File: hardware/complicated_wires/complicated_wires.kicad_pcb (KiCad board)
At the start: 2 copper layers, 80 x 80 mm, 37 parts, among them J1 JST_XH_4P, U1 Pico2

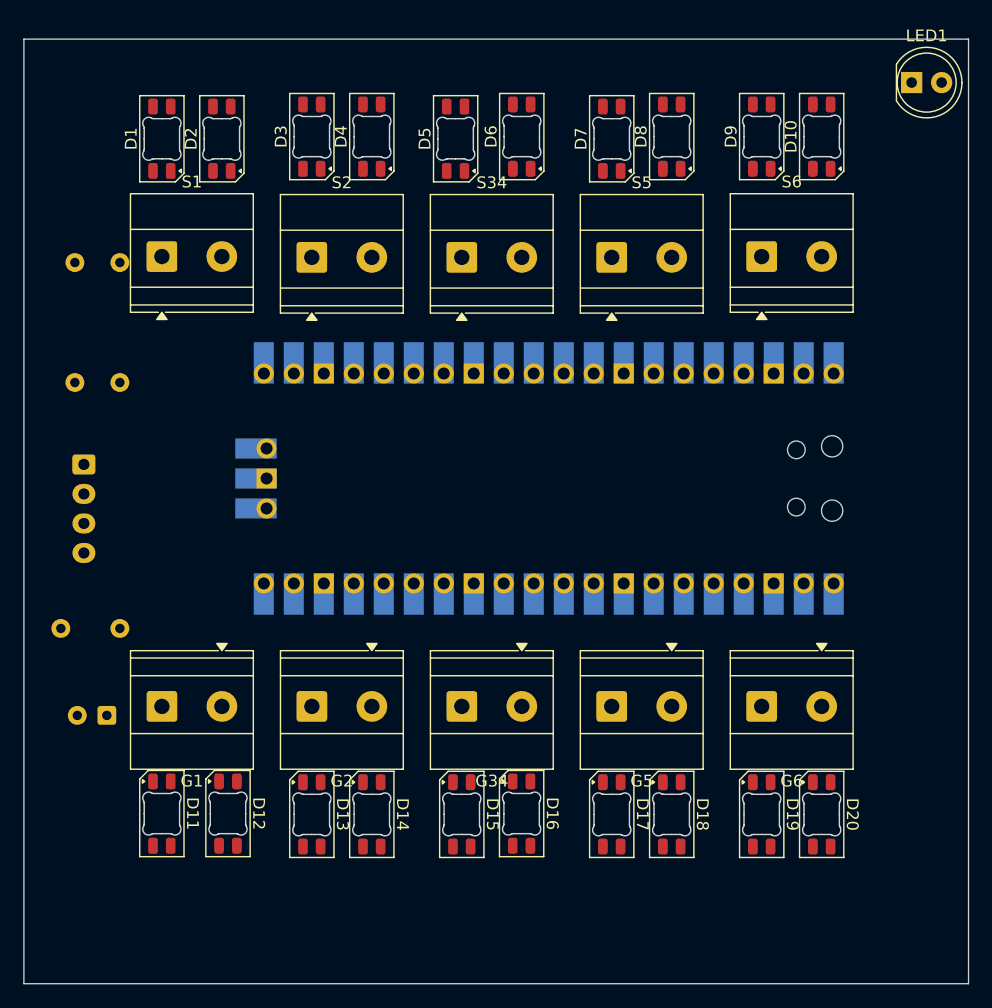
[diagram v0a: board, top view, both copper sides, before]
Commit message: 複雑ワイヤ: PCB配置・配線、ねじ穴4個、端子台フットプリント更新、JLCPCBルール適用
- 端子台をMKDS-1,5-2-5.08(APF-142相当)に変更、GND側のピン番号をS側と揃えた
- 四隅にねじ穴(径2.6mm、縁から9mm)を追加
- 配線完了(未配線0)。DRCエラーはU1/J1のGNDパッドのサーマルスポーク不足7件のみ
- complicated_wires.kicad_dru(LED1の四隅キープアウト例外を含む)を追加

Co-Authored-By: Claude Sonnet 5.5 <noreply@anthropic.com>
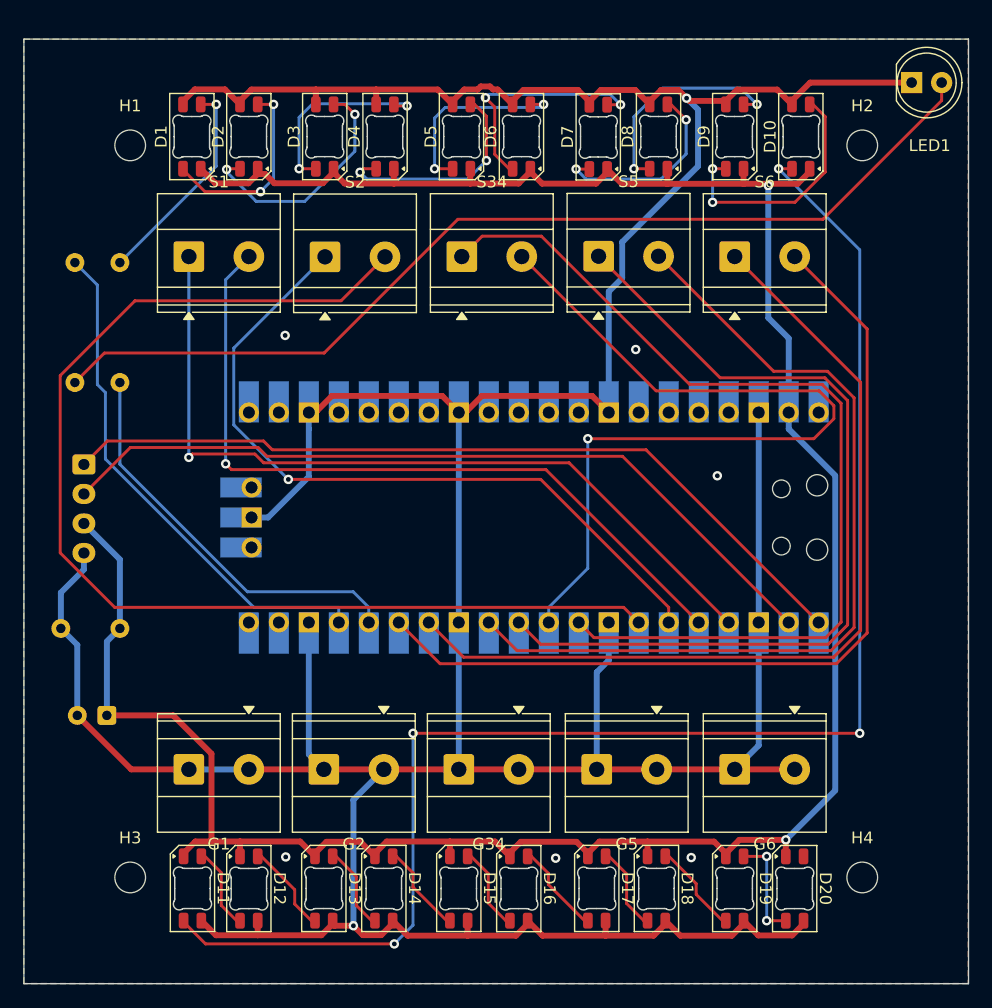
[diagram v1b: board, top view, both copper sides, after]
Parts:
- added H1: MountingHole_2.6mm, MountingHole:MountingHole_2.6mm, F.Cu at (121.8, 38.8)
- added H2: MountingHole_2.6mm, MountingHole:MountingHole_2.6mm, F.Cu at (183.8, 38.8)
- added H3: MountingHole_2.6mm, MountingHole:MountingHole_2.6mm, F.Cu at (121.8, 100.8)
- added H4: MountingHole_2.6mm, MountingHole:MountingHole_2.6mm, F.Cu at (183.8, 100.8)
- moved D11 6.85 mm to (127.1, 101.8)
- moved D19 6.68 mm to (173.0, 101.8)
- moved D20 6.68 mm to (178.1, 101.8)
- moved D12 6.59 mm to (131.8, 101.8)
- moved D18 6.41 mm to (166.3, 101.8)
- moved D17 6.40 mm to (161.3, 101.8)
- moved D13 6.36 mm to (138.2, 101.8)
- moved D14 6.36 mm to (143.3, 101.8)
- moved D16 6.35 mm to (154.7, 101.8)
- moved D15 6.28 mm to (149.6, 101.8)
- moved G6 5.80 mm to (178.1, 91.7)
- moved G1 5.80 mm to (131.8, 91.7)
- moved G5 5.48 mm to (166.4, 91.7)
- moved G2 5.43 mm to (143.3, 91.7)
- moved G34 5.34 mm to (154.7, 91.7)
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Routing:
- net GND: track 0.00 -> 383.5 mm, vias 0 -> 8
- net +5V: track 0.00 -> 219.8 mm, vias 0 -> 2
- net /NP11_DIN: track 0.00 -> 126.8 mm, vias 0 -> 4
- net /WIRE4: track 0.00 -> 98.1 mm
- net Net-(LED1-A): track 0.00 -> 84.8 mm
- net /WIRE5: track 0.00 -> 80.5 mm
- net /WIRE10: track 0.00 -> 76.6 mm
- net /WIRE9: track 0.00 -> 74.8 mm
- net /WIRE7: track 0.00 -> 74.4 mm
- net /WIRE8: track 0.00 -> 73.7 mm
- net /WIRE6: track 0.00 -> 71.2 mm, vias 0 -> 1
- net /UART_TX: track 0.00 -> 69.4 mm
- net /WIRE1: track 0.00 -> 68.8 mm, vias 0 -> 1
- net /UART_RX: track 0.00 -> 67.5 mm
- net /WIRE2: track 0.00 -> 64.0 mm, vias 0 -> 1
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- added copper zone on B.Cu, net GND
- added copper zone on F.Cu, net GND
